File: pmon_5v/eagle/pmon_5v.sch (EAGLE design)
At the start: 28 parts, among them J1 USB, J2 USB, J3 USB_A, J4 PINHD-2X3, Q1 16Mhz, U1 LTC2943, U2 FT232RL, U3 ATMEGA328TQFP32

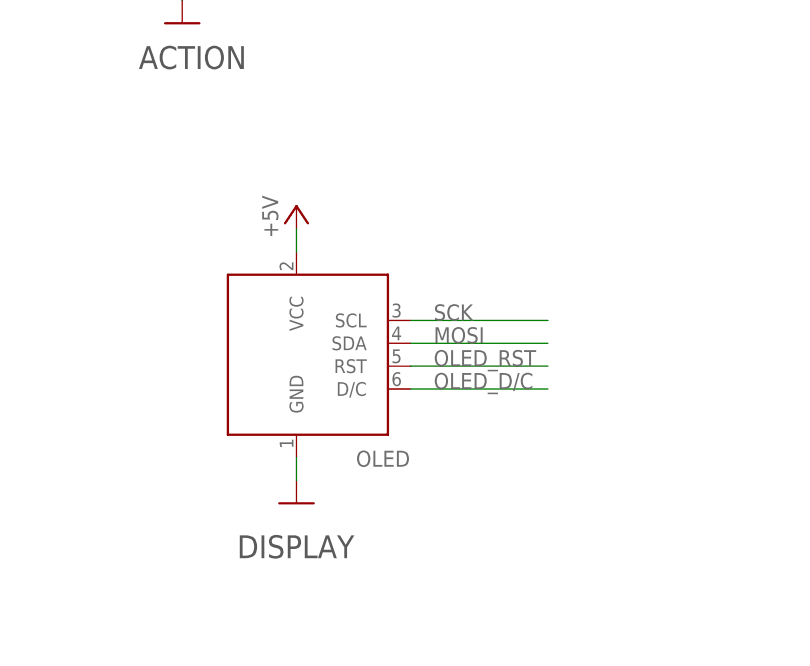
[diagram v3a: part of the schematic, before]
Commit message: Added OLED reset pulldown resistor.
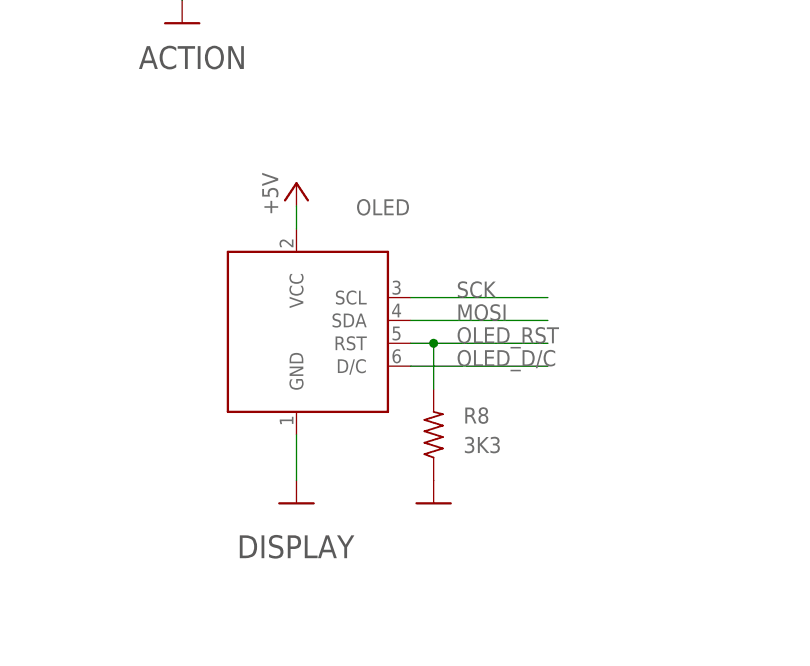
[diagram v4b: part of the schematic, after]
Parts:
- added R8: 3K3, pmon_5v:RES-R0603
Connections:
- net GND: now also R8.1
- net OLED_RST: now also R8.2
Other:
- moved on the sheet: OLED
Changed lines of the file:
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@@
 <part name="U$19" library="pmon_5v" deviceset="NC" device=""/>
 <part name="U$21" library="pmon_5v" deviceset="NC" device=""/>
+<part name="R8" library="pmon_5v" deviceset="RES-" device="R0603" value="3K3"/>
+<part name="GND2" library="pmon_5v" deviceset="GND" device=""/>
 </parts>
 <sheets>
@@
 <attribute name="VALUE" x="44.196" y="212.852" size="1.778" layer="96"/>
 </instance>
-<instance part="OLED" gate="G$1" x="129.54" y="71.12" smashed="yes">
-<attribute name="NAME" x="136.144" y="59.944" size="1.778" layer="95"/>
+<instance part="OLED" gate="G$1" x="129.54" y="73.66" smashed="yes">
+<attribute name="NAME" x="136.144" y="87.884" size="1.778" layer="95"/>
 </instance>
 <instance part="GND33" gate="1" x="129.54" y="55.88" smashed="yes"/>
-<instance part="P+7" gate="1" x="129.54" y="88.9" smashed="yes" rot="MR0">
-<attribute name="VALUE" x="125.73" y="85.344" size="1.778" layer="96" rot="MR90"/>
+<instance part="P+7" gate="1" x="129.54" y="91.44" smashed="yes" rot="MR0">
+<attribute name="VALUE" x="125.73" y="87.884" size="1.778" layer="96" rot="MR90"/>
 </instance>
 <instance part="U$9" gate="G$1" x="238.76" y="162.56" rot="R180"/>
@@
 <instance part="U$19" gate="G$1" x="238.76" y="208.28" rot="R180"/>
 <instance part="U$21" gate="G$1" x="238.76" y="205.74" rot="R180"/>
+<instance part="R8" gate="G$1" x="144.78" y="63.5" smashed="yes" rot="R90">
+<attribute name="NAME" x="148.082" y="64.7446" size="1.778" layer="95"/>
+<attribute name="VALUE" x="148.082" y="61.468" size="1.778" layer="96"/>
+</instance>
+<instance part="GND2" gate="1" x="144.78" y="55.88" smashed="yes"/>
 </instances>
 <busses>
@@
 <segment>
 <pinref part="OLED" gate="G$1" pin="GND"/>
-<wire x1="129.54" y1="60.96" x2="129.54" y2="58.42" width="0.1524" layer="91"/>
+<wire x1="129.54" y1="63.5" x2="129.54" y2="58.42" width="0.1524" layer="91"/>
 <pinref part="GND33" gate="1" pin="GND"/>
+</segment>
+<segment>
+<pinref part="R8" gate="G$1" pin="1"/>
+<pinref part="GND2" gate="1" pin="GND"/>
 </segment>
 </net>
@@
 <segment>
 <pinref part="OLED" gate="G$1" pin="VCC"/>
-<wire x1="129.54" y1="83.82" x2="129.54" y2="86.36" width="0.1524" layer="91"/>
+<wire x1="129.54" y1="86.36" x2="129.54" y2="88.9" width="0.1524" layer="91"/>
 <pinref part="P+7" gate="1" pin="+5V"/>
 </segment>
@@
 <segment>
 <pinref part="OLED" gate="G$1" pin="SCL"/>
-<wire x1="142.24" y1="76.2" x2="157.48" y2="76.2" width="0.1524" layer="91"/>
-<label x="144.78" y="76.2" size="1.778" layer="95"/>
+<wire x1="142.24" y1="78.74" x2="157.48" y2="78.74" width="0.1524" layer="91"/>
+<label x="147.32" y="78.74" size="1.778" layer="95"/>
 </segment>
 <segment>
@@
 <segment>
 <pinref part="OLED" gate="G$1" pin="SDA"/>
-<wire x1="142.24" y1="73.66" x2="157.48" y2="73.66" width="0.1524" layer="91"/>
-<label x="144.78" y="73.66" size="1.778" layer="95"/>
+<wire x1="142.24" y1="76.2" x2="157.48" y2="76.2" width="0.1524" layer="91"/>
+<label x="147.32" y="76.2" size="1.778" layer="95"/>
 </segment>
 <segment>
@@
 <segment>
 <pinref part="OLED" gate="G$1" pin="D/C"/>
-<wire x1="142.24" y1="68.58" x2="157.48" y2="68.58" width="0.1524" layer="91"/>
-<label x="144.78" y="68.58" size="1.778" layer="95"/>
+<wire x1="142.24" y1="71.12" x2="157.48" y2="71.12" width="0.1524" layer="91"/>
+<label x="147.32" y="71.12" size="1.778" layer="95"/>
 </segment>
 </net>
@@
 <segment>
 <pinref part="OLED" gate="G$1" pin="RST"/>
-<wire x1="142.24" y1="71.12" x2="157.48" y2="71.12" width="0.1524" layer="91"/>
-<label x="144.78" y="71.12" size="1.778" layer="95"/>
-</segment>
-</net>
+<wire x1="142.24" y1="73.66" x2="144.78" y2="73.66" width="0.1524" layer="91"/>
+<label x="147.32" y="73.66" size="1.778" layer="95"/>
+<pinref part="R8" gate="G$1" pin="2"/>
+<wire x1="144.78" y1="73.66" x2="157.48" y2="73.66" width="0.1524" layer="91"/>
+<wire x1="144.78" y1="68.58" x2="144.78" y2="73.66" width="0.1524" layer="91"/>
+<junction x="144.78" y="73.66"/>
+</segment>
+</net>

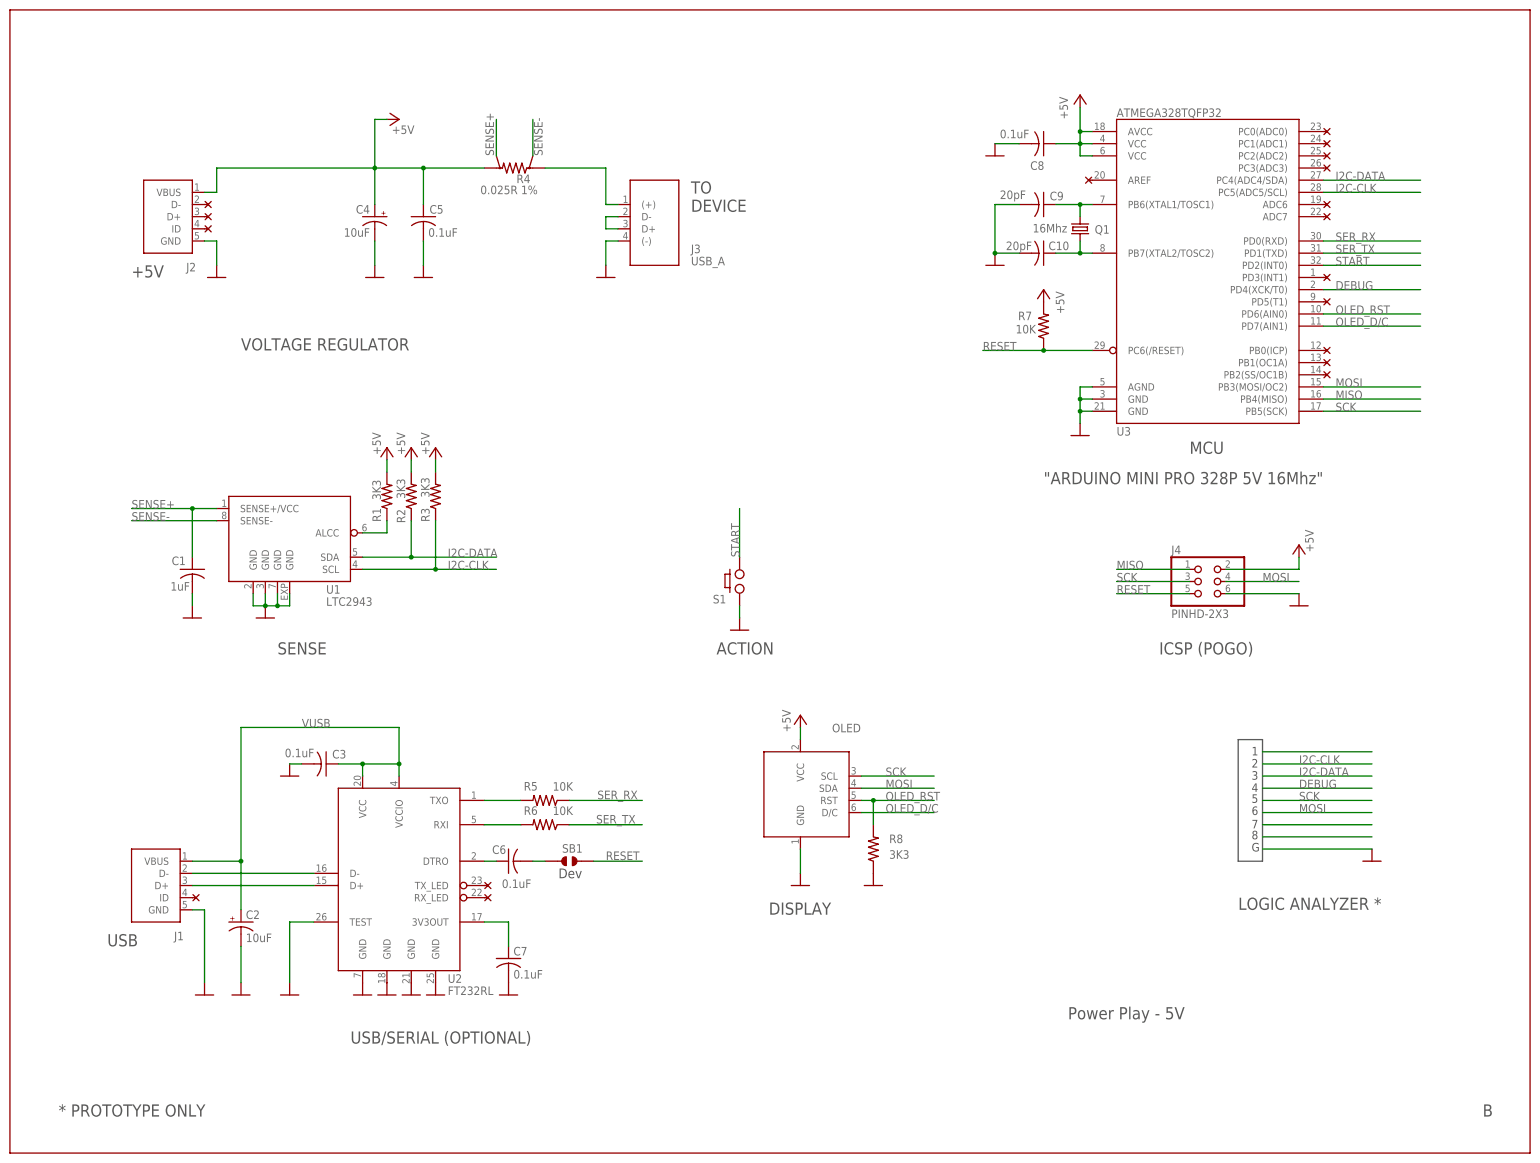
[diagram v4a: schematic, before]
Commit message: Added 4V regulator. Yet to do final auto routing.
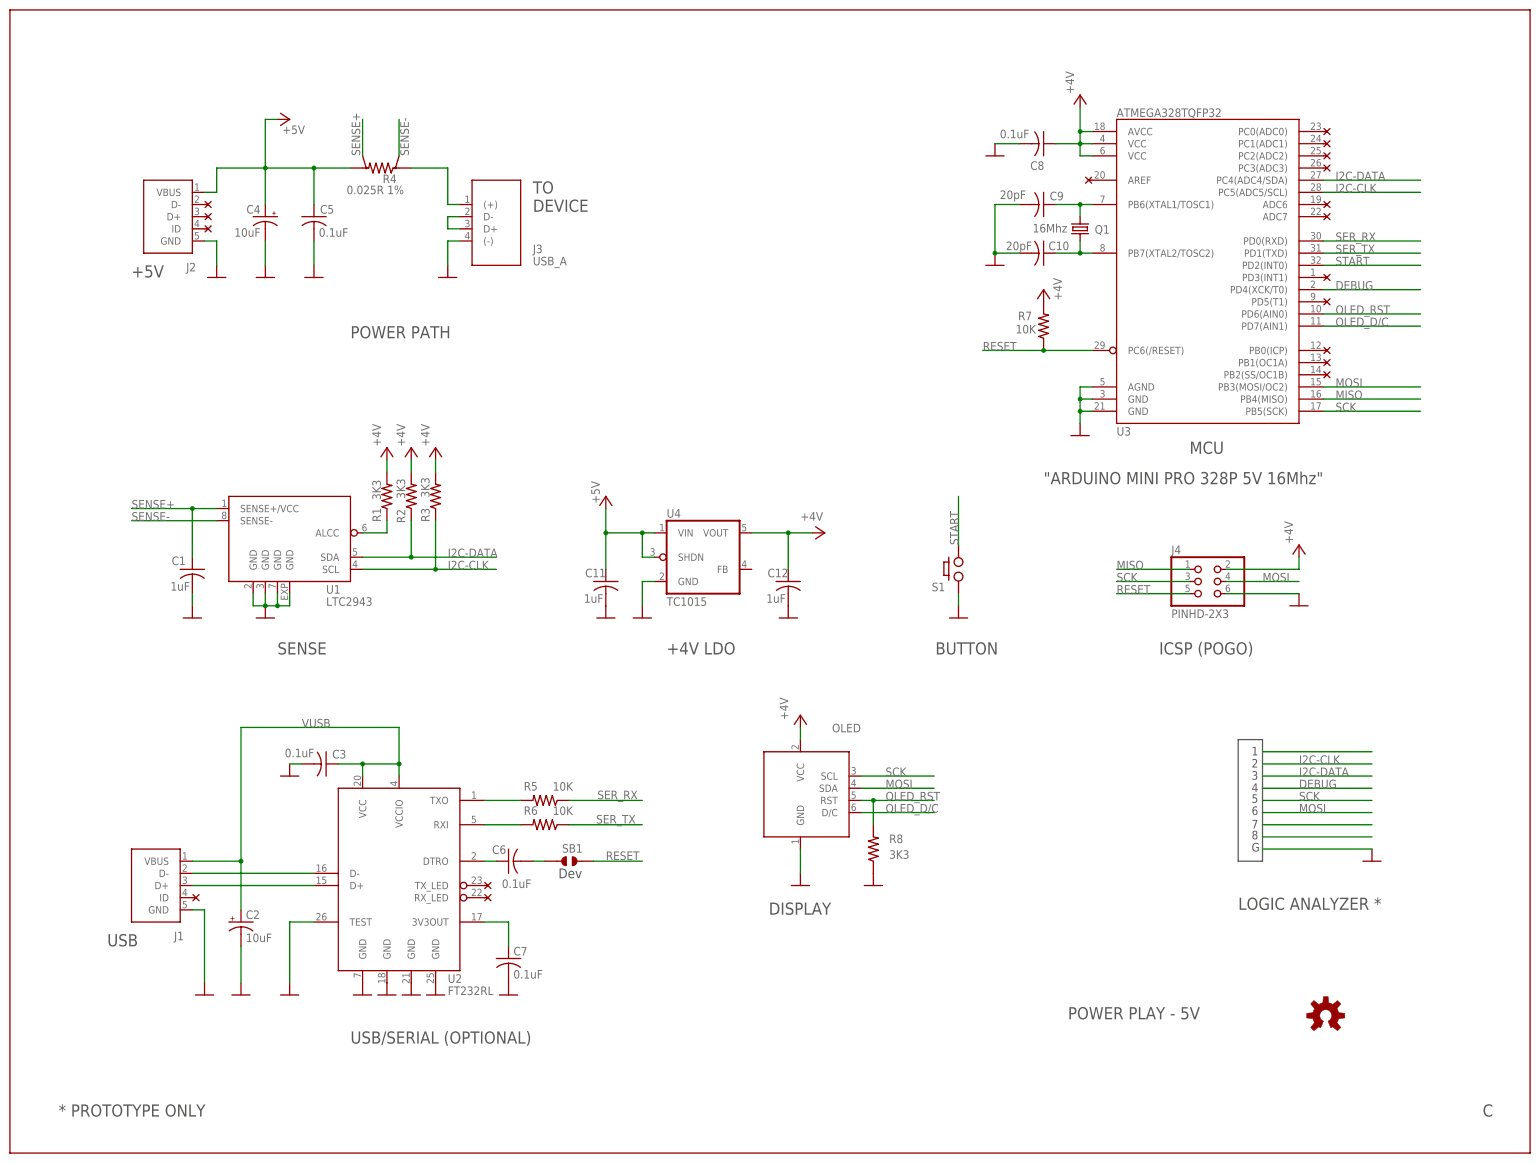
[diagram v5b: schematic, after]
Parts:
- added C11, C12: 1uF, pmon_5v:CAP-C0603
- added U$28: OSH, pmon_5v:OSH
- added U4: TC1015, pmon_5v:TC1015
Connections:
- new net +4V: C12.1, C8.1, J4.2, OLED.VCC, R1.2, R2.2, R3.2, R7.2, U3.AVCC, U3.VCC@1, U3.VCC@2, U4.VOUT
- net +5V: now also C11.1, U4.SHDN, U4.VIN; no longer C8.1, J4.2, OLED.VCC, R1.2, R2.2, R3.2, R7.2, U3.AVCC, U3.VCC@1, U3.VCC@2
- net GND: now also C11.2, C12.2, U4.GND
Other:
- note added: "+4V LDO"
- note added: "BUTTON"
- note added: "C"
- note added: "POWER PATH"
- note added: "POWER PLAY - 5V"
- note removed: "ACTION"
- note removed: "B"
- note removed: "Power Play - 5V"
- note removed: "VOLTAGE REGULATOR"
- moved on the sheet: C4, C5, J3, R4, S1
